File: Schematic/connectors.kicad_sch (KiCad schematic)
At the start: 32 parts, among them J10 PIN2216, J11 PIN2216, J12 PIN2216, J2 PIN2216, J3 PIN2216, J4 PIN2216, J5 PIN2216, J6 PIN2216, J7 PIN2216, J8 PIN2216, J9 PIN2216, U10 HDGC1002WR-S-4P, U11 HDGC1002WR-S-4P, U14 HDGC1002WR-S-4P, U15 HDGC1002WR-S-6P, U16 HDGC1002WR-S-8P, U17 HDGC1002WR-S-8P, U7 HDGC1002WR-S-4P, U8 HDGC1002WR-S-4P, U9 HDGC1002WR-S-4P

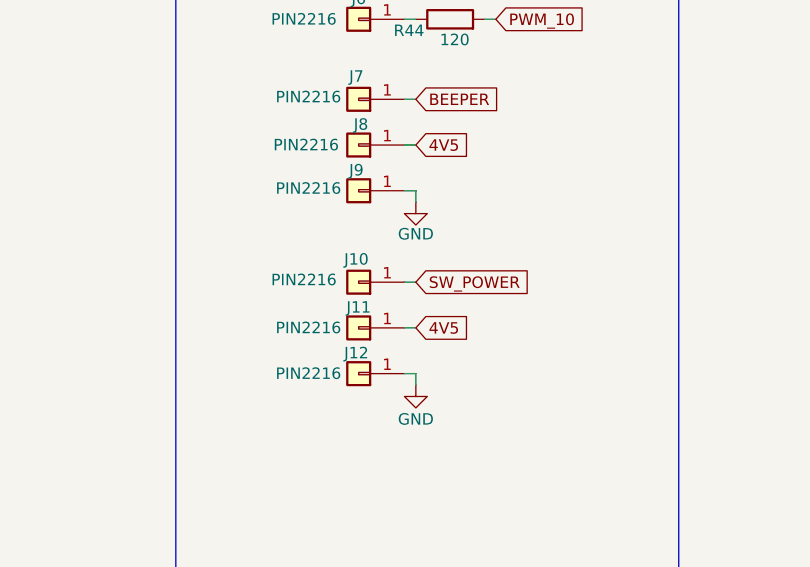
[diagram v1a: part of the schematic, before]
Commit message: finished every routing and fix errors in DRC
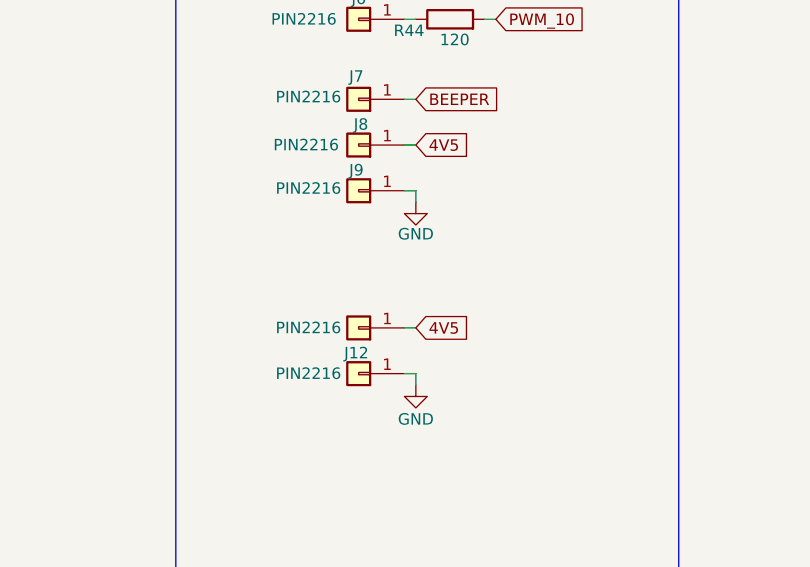
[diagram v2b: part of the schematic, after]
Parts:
- removed J10: PIN2216, fch7_fp:SolderPad_1x01_SMD_2.2x1.6mm, symbol Connector_Generic:Conn_01x01
- J11, J12, J2, J3, J4, J5, J6, J7, J8, J9: footprint fch7_fp:SolderPad_1x01_SMD_2.2x1.6mm -> fch7:SolderPad_1x01_SMD_2.2x1.6mm
- RN1, RN2: footprint fch7_fp:RES-ARRAY-SMD_0603-8P-L3.2-W1.6-BL -> fch7:RES-ARRAY-SMD_0603-8P-L3.2-W1.6-BL
- TP1, TP2, TP3, TP4, TP5, TP6, TP7: footprint fch7_fp:TestPoint_Pad_D0.8 -> fch7:TestPoint_Pad_D0.8
- U10, U11, U14, U7, U8, U9: footprint fch7_fp:CONN-SMD_4P-P1.00_HDGC_HDGC1002WR-S-4P -> fch7:CONN-SMD_4P-P1.00_HDGC_HDGC1002WR-S-4P
- U15: footprint fch7_fp:CONN-SMD_HDGC1002WR-S-6P -> fch7:CONN-SMD_HDGC1002WR-S-6P
- U16, U17: footprint fch7_fp:CONN-SMD_HDGC1002WR-S-8P -> fch7:CONN-SMD_HDGC1002WR-S-8P
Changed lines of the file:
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@@
 	(wire
 		(pts
-			(xy 134.62 160.02) (xy 135.89 160.02)
-		)
-		(stroke
-			(width 0)
-			(type default)
-		)
-	)
-	(wire
-		(pts
 			(xy 269.24 53.34) (xy 270.51 53.34)
 		)
@@
 		)
 	)
-	(global_label "SW_POWER"
-		(shape input)
-		(at 135.89 160.02 0)
-		(fields_autoplaced yes)
-		(effects
-			(font
-				(size 1.27 1.27)
-			)
-			(justify left)
-		)
-		(property "Intersheetrefs" "${INTERSHEET_REFS}"
-			(at 148.9746 160.02 0)
-			(effects
-				(font
-					(size 1.27 1.27)
-				)
-				(justify left)
-				(hide yes)
-			)
-		)
-	)
 	(global_label "4V5"
 		(shape input)
@@
 			)
 		)
-		(property "Footprint" "fch7_fp:TestPoint_Pad_D0.8"
+		(property "Footprint" "fch7:TestPoint_Pad_D0.8"
 			(at 265.43 149.86 0)
 			(effects
@@
 			)
 		)
-		(property "Footprint" "fch7_fp:CONN-SMD_4P-P1.00_HDGC_HDGC1002WR-S-4P"
+		(property "Footprint" "fch7:CONN-SMD_4P-P1.00_HDGC_HDGC1002WR-S-4P"
 			(at 33.02 105.41 0)
 			(effects
@@
 			)
 		)
-		(property "Footprint" "fch7_fp:SolderPad_1x01_SMD_2.2x1.6mm"
+		(property "Footprint" "fch7:SolderPad_1x01_SMD_2.2x1.6mm"
 			(at 129.54 111.76 0)
 			(effects
@@
 			)
 		)
-		(property "Footprint" "fch7_fp:TestPoint_Pad_D0.8"
+		(property "Footprint" "fch7:TestPoint_Pad_D0.8"
 			(at 237.49 154.94 0)
 			(effects
@@
 			)
 		)
-		(property "Footprint" "fch7_fp:RES-ARRAY-SMD_0603-8P-L3.2-W1.6-BL"
+		(property "Footprint" "fch7:RES-ARRAY-SMD_0603-8P-L3.2-W1.6-BL"
 			(at 263.652 106.426 0)
 			(effects
@@
 			)
 		)
-		(property "Footprint" "fch7_fp:TestPoint_Pad_D0.8"
+		(property "Footprint" "fch7:TestPoint_Pad_D0.8"
 			(at 237.49 125.73 0)
 			(effects
@@
 			)
 		)
-		(property "Footprint" "fch7_fp:CONN-SMD_HDGC1002WR-S-6P"
+		(property "Footprint" "fch7:CONN-SMD_HDGC1002WR-S-6P"
 			(at 184.15 41.91 0)
 			(effects
@@
 			)
 		)
-		(property "Footprint" "fch7_fp:CONN-SMD_4P-P1.00_HDGC_HDGC1002WR-S-4P"
+		(property "Footprint" "fch7:CONN-SMD_4P-P1.00_HDGC_HDGC1002WR-S-4P"
 			(at 33.02 73.66 0)
 			(effects
@@
 			)
 		)
-		(property "Footprint" "fch7_fp:SolderPad_1x01_SMD_2.2x1.6mm"
+		(property "Footprint" "fch7:SolderPad_1x01_SMD_2.2x1.6mm"
 			(at 129.54 116.84 0)
 			(effects
@@
 			)
 		)
-		(property "Footprint" "fch7_fp:CONN-SMD_4P-P1.00_HDGC_HDGC1002WR-S-4P"
+		(property "Footprint" "fch7:CONN-SMD_4P-P1.00_HDGC_HDGC1002WR-S-4P"
 			(at 184.15 82.55 0)
 			(effects
@@
 			)
 		)
-		(property "Footprint" "fch7_fp:TestPoint_Pad_D0.8"
+		(property "Footprint" "fch7:TestPoint_Pad_D0.8"
 			(at 237.49 135.89 0)
 			(effects
@@
 					(size 1.27 1.27)
 				)
+				(hide yes)
 			)
 		)
@@
 			)
 		)
-		(property "Footprint" "fch7_fp:SolderPad_1x01_SMD_2.2x1.6mm"
+		(property "Footprint" "fch7:SolderPad_1x01_SMD_2.2x1.6mm"
 			(at 129.54 165.1 0)
 			(effects
@@
 			)
 		)
-		(property "Footprint" "fch7_fp:TestPoint_Pad_D0.8"
+		(property "Footprint" "fch7:TestPoint_Pad_D0.8"
 			(at 265.43 129.54 0)
 			(effects
@@
 			)
 		)
-		(property "Footprint" "fch7_fp:CONN-SMD_4P-P1.00_HDGC_HDGC1002WR-S-4P"
+		(property "Footprint" "fch7:CONN-SMD_4P-P1.00_HDGC_HDGC1002WR-S-4P"
 			(at 33.02 138.43 0)
 			(effects
@@
 			)
 		)
-		(property "Footprint" "fch7_fp:CONN-SMD_4P-P1.00_HDGC_HDGC1002WR-S-4P"
+		(property "Footprint" "fch7:CONN-SMD_4P-P1.00_HDGC_HDGC1002WR-S-4P"
 			(at 33.02 40.64 0)
 			(effects
@@
 	)
 	(symbol
-		(lib_id "Connector_Generic:Conn_01x01")
-		(at 129.54 160.02 180)
-		(unit 1)
-		(exclude_from_sim no)
-		(in_bom yes)
-		(on_board yes)
-		(dnp no)
-		(property "Reference" "J10"
-			(at 129.286 157.48 0)
-			(effects
-				(font
-					(size 1.27 1.27)
-				)
-			)
-		)
-		(property "Value" "PIN2216"
-			(at 123.444 159.766 0)
-			(effects
-				(font
-					(size 1.27 1.27)
-				)
-			)
-		)
-		(property "Footprint" "fch7_fp:SolderPad_1x01_SMD_2.2x1.6mm"
-			(at 129.54 160.02 0)
-			(effects
-				(font
-					(size 1.27 1.27)
-				)
-				(hide yes)
-			)
-		)
-		(property "Datasheet" "~"
-			(at 129.54 160.02 0)
-			(effects
-				(font
-					(size 1.27 1.27)
-				)
-				(hide yes)
-			)
-		)
-		(property "Description" "Generic connector, single row, 01x01, script generated (kicad-library-utils/schlib/autogen/connector/)"
-			(at 129.54 160.02 0)
-			(effects
-				(font
-					(size 1.27 1.27)
-				)
-				(hide yes)
-			)
-		)
-		(property "Fréquence" ""
-			(at 129.54 160.02 0)
-			(effects
-				(font
-					(size 1.27 1.27)
-				)
-				(hide yes)
-			)
-		)
-		(property "MPN" "~"
-			(at 129.54 160.02 0)
-			(effects
-				(font
-					(size 1.27 1.27)
-				)
-				(hide yes)
-			)
-		)
-		(property "Manufacturer" "~"
-			(at 129.54 160.02 0)
-			(effects
-				(font
-					(size 1.27 1.27)
-				)
-				(hide yes)
-			)
-		)
-		(pin "1"
-		)
-		(instances
-			(project "fch7"
-				(path "/11716af6-0e6e-444b-b738-3f12da23c1a2/304e7e23-68f8-4a1f-930d-8ec3265ffbba"
-					(reference "J10")
-					(unit 1)
-				)
-			)
-		)
-	)
-	(symbol
 		(lib_id "power:GND")
 		(at 135.89 118.11 0)
@@
 			)
 		)
-		(property "Footprint" "fch7_fp:TestPoint_Pad_D0.8"
+		(property "Footprint" "fch7:TestPoint_Pad_D0.8"
 			(at 237.49 144.78 0)
 			(effects
@@
 			)
 		)
-		(property "Footprint" "fch7_fp:SolderPad_1x01_SMD_2.2x1.6mm"
+		(property "Footprint" "fch7:SolderPad_1x01_SMD_2.2x1.6mm"
 			(at 129.54 139.7 0)
 			(effects
@@
 			)
 		)
-		(property "Footprint" "fch7_fp:SolderPad_1x01_SMD_2.2x1.6mm"
+		(property "Footprint" "fch7:SolderPad_1x01_SMD_2.2x1.6mm"
 			(at 129.54 149.86 0)
 			(effects
@@
 			)
 		)
-		(property "Footprint" "fch7_fp:CONN-SMD_4P-P1.00_HDGC_HDGC1002WR-S-4P"
+		(property "Footprint" "fch7:CONN-SMD_4P-P1.00_HDGC_HDGC1002WR-S-4P"
 			(at 33.02 172.72 0)
 			(effects
@@
 			)
 		)
-		(property "Footprint" "fch7_fp:RES-ARRAY-SMD_0603-8P-L3.2-W1.6-BL"
+		(property "Footprint" "fch7:RES-ARRAY-SMD_0603-8P-L3.2-W1.6-BL"
 			(at 262.382 72.136 0)
 			(effects
@@
 			)
 		)
-		(property "Footprint" "fch7_fp:TestPoint_Pad_D0.8"
+		(property "Footprint" "fch7:TestPoint_Pad_D0.8"
 			(at 265.43 139.7 0)
 			(effects
@@
 			)
 		)
-		(property "Footprint" "fch7_fp:SolderPad_1x01_SMD_2.2x1.6mm"
+		(property "Footprint" "fch7:SolderPad_1x01_SMD_2.2x1.6mm"
 			(at 129.54 144.78 0)
 			(effects
@@
 			)
 		)
-		(property "Footprint" "fch7_fp:CONN-SMD_HDGC1002WR-S-8P"
+		(property "Footprint" "fch7:CONN-SMD_HDGC1002WR-S-8P"
 			(at 236.22 60.96 0)
 			(effects
@@
 			)
 		)
-		(property "Footprint" "fch7_fp:SolderPad_1x01_SMD_2.2x1.6mm"
+		(property "Footprint" "fch7:SolderPad_1x01_SMD_2.2x1.6mm"
 			(at 129.54 130.81 0)
 			(effects
@@
 			)
 		)
-		(property "Footprint" "fch7_fp:SolderPad_1x01_SMD_2.2x1.6mm"
+		(property "Footprint" "fch7:SolderPad_1x01_SMD_2.2x1.6mm"
 			(at 129.54 125.73 0)
 			(effects
@@
 			)
 		)
-		(property "Footprint" "fch7_fp:SolderPad_1x01_SMD_2.2x1.6mm"
+		(property "Footprint" "fch7:SolderPad_1x01_SMD_2.2x1.6mm"
 			(at 129.54 170.18 0)
 			(effects
@@
 			)
 		)
-		(property "Footprint" "fch7_fp:CONN-SMD_HDGC1002WR-S-8P"
+		(property "Footprint" "fch7:CONN-SMD_HDGC1002WR-S-8P"
 			(at 241.3 95.25 0)
 			(effects
@@
 			)
 		)
-		(property "Footprint" "fch7_fp:SolderPad_1x01_SMD_2.2x1.6mm"
+		(property "Footprint" "fch7:SolderPad_1x01_SMD_2.2x1.6mm"
 			(at 129.54 106.68 0)
 			(effects

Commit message: Update schematic properties and model paths - Added MPN and Manufacturer properties for ICM-42688-P and MPU-6500 in sensors.kicad_sch. - Changed model paths to use the ${FCH7_3DMODEL_DIR} variable for various components in the fch7.pretty library. - Added a 3D model for the SOD-123 component.
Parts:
- RN1, RN2: MPN (none) -> 4D03WGJ0101T5E
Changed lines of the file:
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@@
+			)
+		)
+		(property "MPN" "4D03WGJ0101T5E"
+			(at 261.62 91.44 0)
+			(effects
+				(font
+					(size 1.27 1.27)
+				)
+				(hide yes)
 			)
 		)
@@
 			(effects
 				(font
+					(size 1.27 1.27)
+				)
+				(hide yes)
+			)
+		)
+		(property "MPN" "4D03WGJ0101T5E"
+			(at 260.35 57.15 0)
+			(effects
+				(font

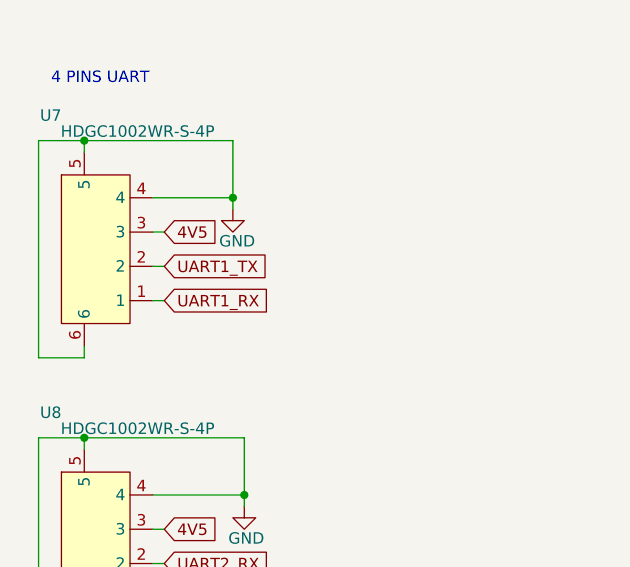
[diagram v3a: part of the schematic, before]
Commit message: compacting in 40mm wide format the board
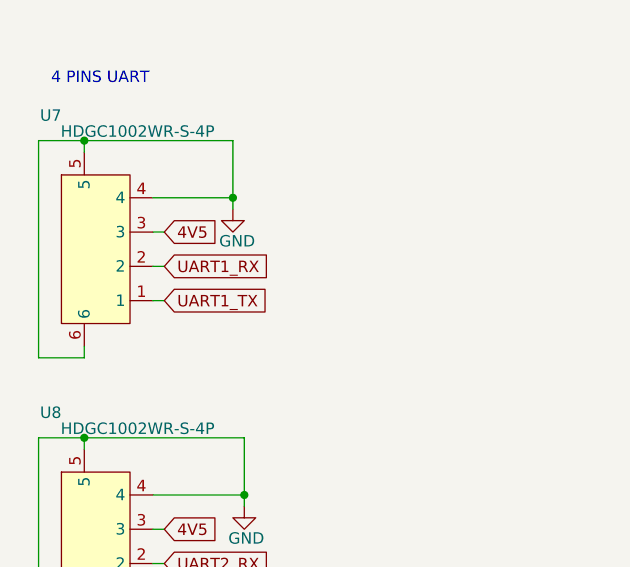
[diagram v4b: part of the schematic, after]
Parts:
- J11, J12, J2, J3, J4, J5, J6, J7, J8, J9: footprint fch7:SolderPad_1x01_SMD_2.2x1.6mm -> fch7:SolderPad_1x01_SMD_1.2x1.6mm
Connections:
- net UART1_RX: now also U7.2; no longer U7.1
- net UART1_TX: now also U7.1; no longer U7.2
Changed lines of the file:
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@@
 	(global_label "UART1_TX"
 		(shape input)
-		(at 40.64 43.18 0)
+		(at 40.64 46.99 0)
 		(fields_autoplaced yes)
 		(effects
@@
 		)
 		(property "Intersheetrefs" "${INTERSHEET_REFS}"
-			(at 52.6361 43.18 0)
+			(at 52.6361 46.99 0)
 			(effects
 				(font
@@
 	(global_label "UART1_RX"
 		(shape input)
-		(at 40.64 46.99 0)
+		(at 40.64 43.18 0)
 		(fields_autoplaced yes)
 		(effects
@@
 		)
 		(property "Intersheetrefs" "${INTERSHEET_REFS}"
-			(at 52.9385 46.99 0)
+			(at 52.9385 43.18 0)
 			(effects
 				(font
@@
 			)
 		)
-		(property "Footprint" "fch7:SolderPad_1x01_SMD_2.2x1.6mm"
+		(property "Footprint" "fch7:SolderPad_1x01_SMD_1.2x1.6mm"
 			(at 129.54 111.76 0)
 			(effects
@@
 			)
 		)
-		(property "Footprint" "fch7:SolderPad_1x01_SMD_2.2x1.6mm"
+		(property "Footprint" "fch7:SolderPad_1x01_SMD_1.2x1.6mm"
 			(at 129.54 116.84 0)
 			(effects
@@
 			)
 		)
-		(property "Footprint" "fch7:SolderPad_1x01_SMD_2.2x1.6mm"
+		(property "Footprint" "fch7:SolderPad_1x01_SMD_1.2x1.6mm"
 			(at 129.54 165.1 0)
 			(effects
@@
 			)
 		)
-		(property "Footprint" "fch7:SolderPad_1x01_SMD_2.2x1.6mm"
+		(property "Footprint" "fch7:SolderPad_1x01_SMD_1.2x1.6mm"
 			(at 129.54 139.7 0)
 			(effects
@@
 			)
 		)
-		(property "Footprint" "fch7:SolderPad_1x01_SMD_2.2x1.6mm"
+		(property "Footprint" "fch7:SolderPad_1x01_SMD_1.2x1.6mm"
 			(at 129.54 149.86 0)
 			(effects
@@
 			)
 		)
-		(property "Footprint" "fch7:SolderPad_1x01_SMD_2.2x1.6mm"
+		(property "Footprint" "fch7:SolderPad_1x01_SMD_1.2x1.6mm"
 			(at 129.54 144.78 0)
 			(effects
@@
 			)
 		)
-		(property "Footprint" "fch7:SolderPad_1x01_SMD_2.2x1.6mm"
+		(property "Footprint" "fch7:SolderPad_1x01_SMD_1.2x1.6mm"
 			(at 129.54 130.81 0)
 			(effects
@@
 			)
 		)
-		(property "Footprint" "fch7:SolderPad_1x01_SMD_2.2x1.6mm"
+		(property "Footprint" "fch7:SolderPad_1x01_SMD_1.2x1.6mm"
 			(at 129.54 125.73 0)
 			(effects
@@
 			)
 		)
-		(property "Footprint" "fch7:SolderPad_1x01_SMD_2.2x1.6mm"
+		(property "Footprint" "fch7:SolderPad_1x01_SMD_1.2x1.6mm"
 			(at 129.54 170.18 0)
 			(effects
@@
 			)
 		)
-		(property "Footprint" "fch7:SolderPad_1x01_SMD_2.2x1.6mm"
+		(property "Footprint" "fch7:SolderPad_1x01_SMD_1.2x1.6mm"
 			(at 129.54 106.68 0)
 			(effects

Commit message: minor update
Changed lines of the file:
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@@
 	(polyline
 		(pts
-			(xy 109.22 13.97) (xy 109.22 199.39)
+			(xy 101.6 12.7) (xy 101.6 198.12)
 		)
 		(stroke
@@
 				)
 			)
-			(table_cell "UART6 WIFI"
+			(table_cell "UART6 RX"
 				(exclude_from_sim no)
 				(at 67.31 71.12 0)
@@
 				)
 			)
-			(table_cell "UART7 ESC for telemetry bi-directional"
+			(table_cell "UART7 ESC feedback for telemetry bi-directional"
 				(exclude_from_sim no)
 				(at 67.31 76.2 0)

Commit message: minor update and some checking
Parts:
- RN1, RN2: value 100Ω -> 100
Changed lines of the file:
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@@
 			)
 		)
-		(property "Value" "100Ω"
+		(property "Value" "100"
 			(at 262.382 99.314 0)
 			(effects
@@
 			)
 		)
-		(property "Value" "100Ω"
+		(property "Value" "100"
 			(at 261.112 65.024 0)
 			(effects

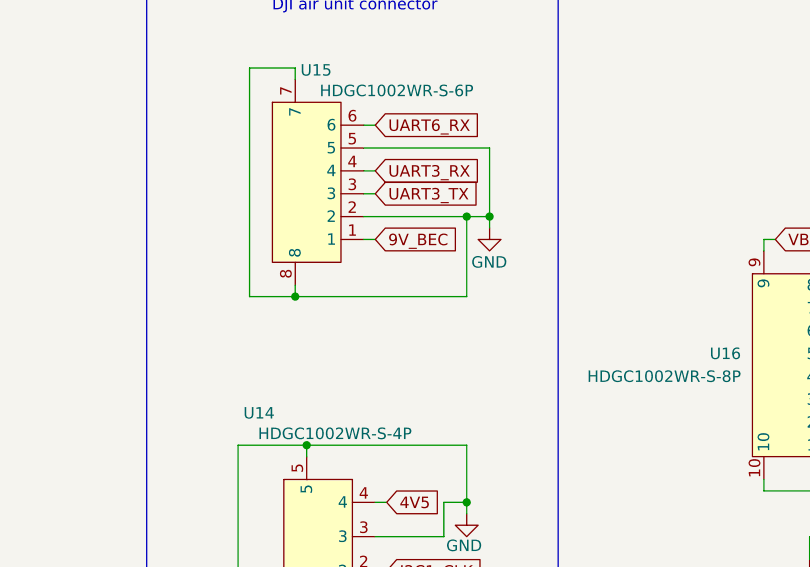
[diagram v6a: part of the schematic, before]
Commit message: remove switch to use jumper for bootloader activation
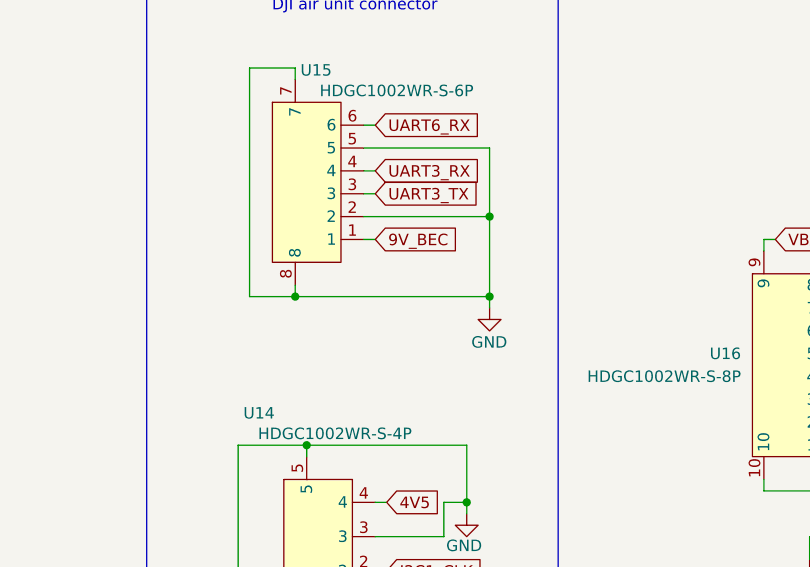
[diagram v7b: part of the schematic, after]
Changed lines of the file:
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@@
 	)
 	(junction
-		(at 200.66 45.72)
-		(diameter 0)
-		(color 0 0 0 0)
-	)
-	(junction
 		(at 31.75 62.23)
 		(diameter 0)
@@
 	)
 	(junction
-		(at 203.2 45.72)
-		(diameter 0)
-		(color 0 0 0 0)
-	)
-	(junction
 		(at 31.75 118.11)
 		(diameter 0)
@@
 	)
 	(junction
+		(at 203.2 54.61)
+		(diameter 0)
+		(color 0 0 0 0)
+	)
+	(junction
 		(at 31.75 29.21)
 		(diameter 0)
@@
 	)
 	(junction
+		(at 203.2 45.72)
+		(diameter 0)
+		(color 0 0 0 0)
+	)
+	(junction
 		(at 243.84 68.58)
 		(diameter 0)
@@
 	(wire
 		(pts
-			(xy 189.23 45.72) (xy 200.66 45.72)
-		)
-		(stroke
-			(width 0)
-			(type default)
-		)
-	)
-	(wire
-		(pts
 			(xy 269.24 58.42) (xy 270.51 58.42)
 		)
@@
 	(wire
 		(pts
-			(xy 181.61 54.61) (xy 200.66 54.61)
+			(xy 181.61 54.61) (xy 203.2 54.61)
 		)
 		(stroke
@@
 	(wire
 		(pts
-			(xy 203.2 45.72) (xy 200.66 45.72)
+			(xy 189.23 45.72) (xy 203.2 45.72)
 		)
 		(stroke
@@
 	(wire
 		(pts
+			(xy 203.2 45.72) (xy 203.2 54.61)
+		)
+		(stroke
+			(width 0)
+			(type default)
+		)
+	)
+	(wire
+		(pts
 			(xy 270.51 87.63) (xy 271.78 87.63)
 		)
@@
 	(wire
 		(pts
-			(xy 203.2 46.99) (xy 203.2 45.72)
+			(xy 203.2 55.88) (xy 203.2 54.61)
 		)
 		(stroke
@@
 	(wire
 		(pts
-			(xy 200.66 45.72) (xy 200.66 54.61)
-		)
-		(stroke
-			(width 0)
-			(type default)
-		)
-	)
-	(wire
-		(pts
 			(xy 240.03 110.49) (xy 238.76 110.49)
 		)
@@
 	(symbol
 		(lib_id "power:GND")
-		(at 203.2 46.99 0)
+		(at 203.2 55.88 0)
 		(unit 1)
 		(exclude_from_sim no)
@@
 		(dnp no)
 		(property "Reference" "#PWR063"
-			(at 203.2 53.34 0)
+			(at 203.2 62.23 0)
 			(effects
 				(font
@@
 		)
 		(property "Value" "GND"
-			(at 201.168 50.8 0)
+			(at 201.168 59.69 0)
 			(effects
 				(font
@@
 		)
 		(property "Footprint" ""
-			(at 203.2 46.99 0)
+			(at 203.2 55.88 0)
 			(effects
 				(font
@@
 		)
 		(property "Datasheet" ""
-			(at 203.2 46.99 0)
+			(at 203.2 55.88 0)
 			(effects
 				(font
@@
 		)
 		(property "Description" "Power symbol creates a global label with name \"GND\" , ground"
-			(at 203.2 46.99 0)
+			(at 203.2 55.88 0)
 			(effects
 				(font
